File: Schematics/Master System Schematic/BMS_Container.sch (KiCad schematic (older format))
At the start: 8 parts, among them K1 Cooling Pump Shutoff Relay, K53 BMS_PWR_Relay, K54 Cooling Pump Relay, K55 BMS_Fan_Relay, U6 OrionBMS2

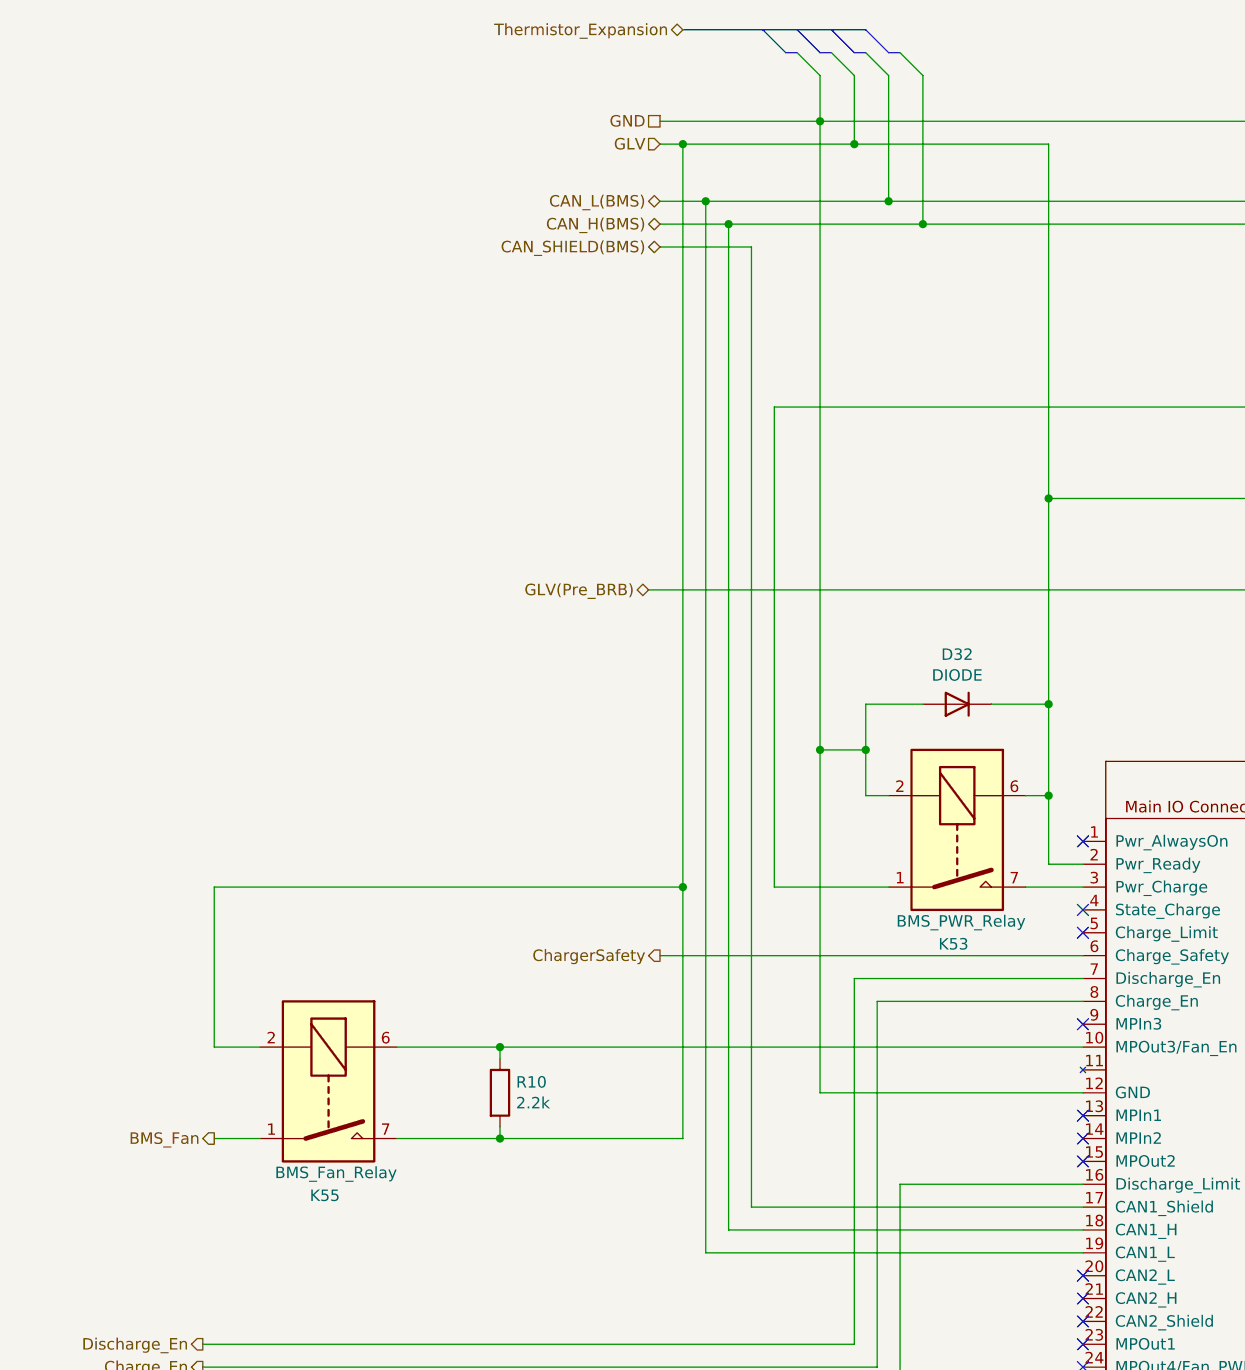
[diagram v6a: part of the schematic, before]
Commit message: Removed BMS fan
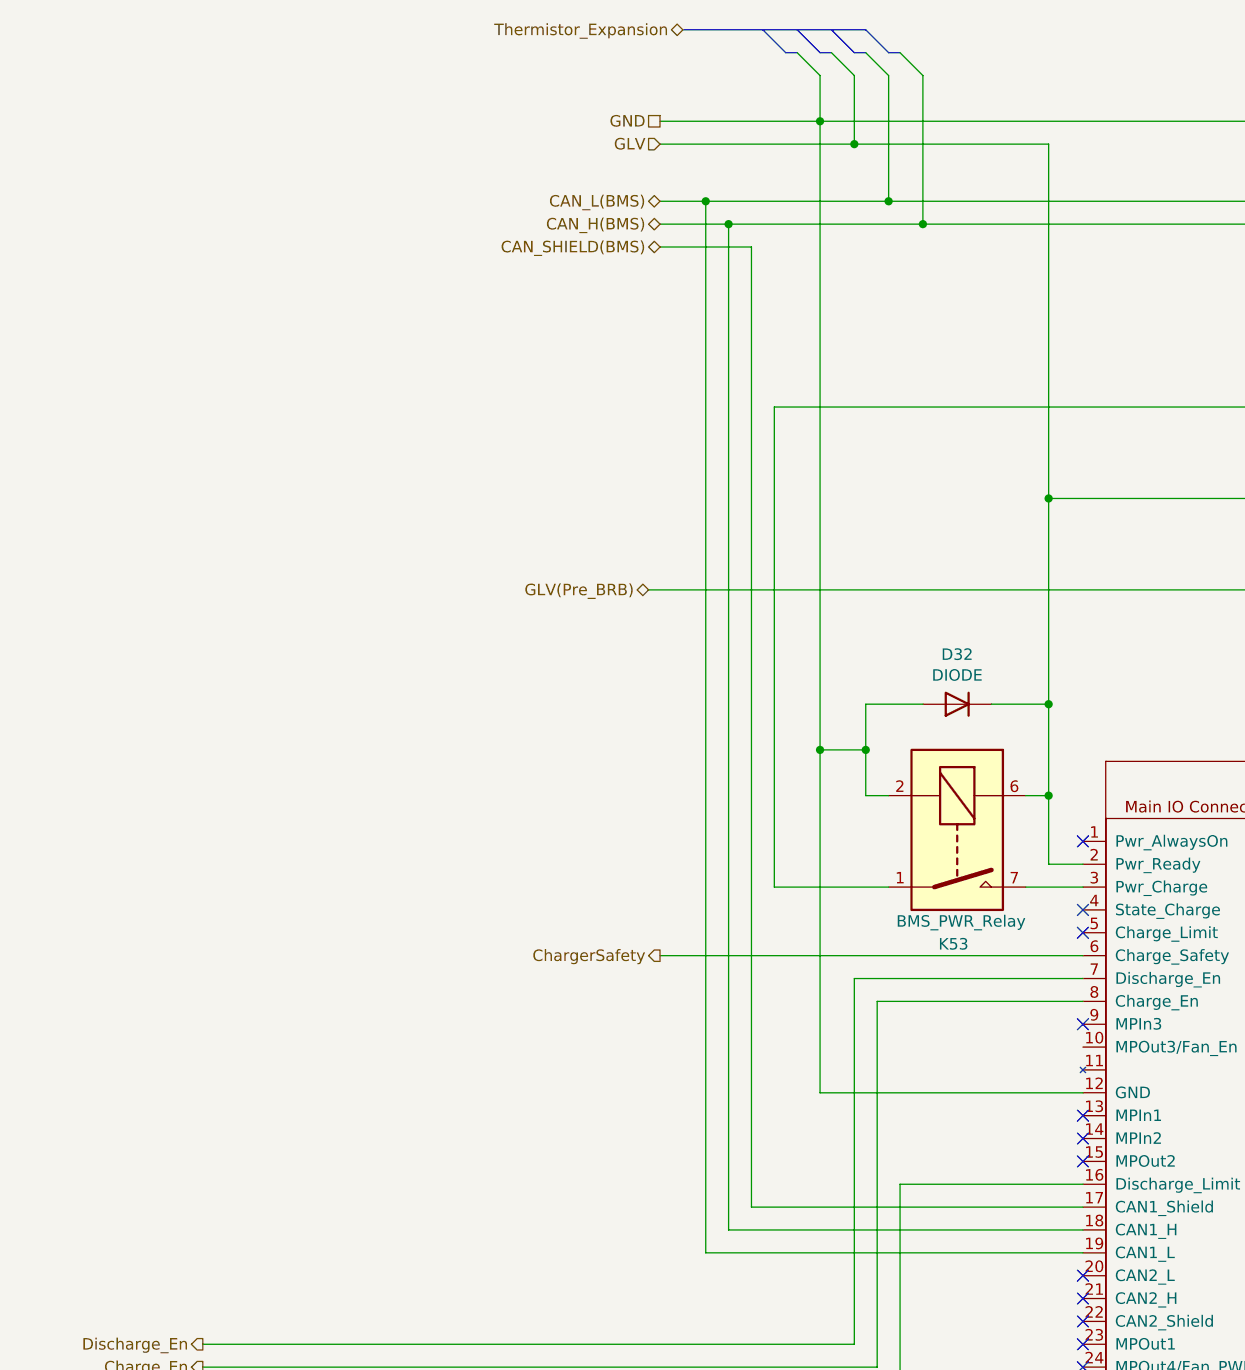
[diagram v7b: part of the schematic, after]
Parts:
- removed K55: BMS_Fan_Relay, Relay_THT:Relay_StandexMeder_DIP_LowProfile, symbol Relay:DIPxx-1Axx-11x
- removed R10: 2.2k, symbol Device:R
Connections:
- net at U6.3 (RM2+): now also K53.7, K53.8
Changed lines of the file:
@@
 	5550 1550 5550 4300
 Connection ~ 5550 1550
-Wire Wire Line
-	4850 1650 4950 1650
 Connection ~ 6550 4100
 Wire Wire Line
@@
 Wire Wire Line
 	8000 1650 8000 2800
-Wire Wire Line
-	6700 5600 4150 5600
-Text HLabel 2900 6000 0    50   Output ~ 0
-BMS_Fan
-Wire Wire Line
-	3100 6000 2900 6000
-Wire Wire Line
-	3700 6000 4150 6000
-Wire Wire Line
-	4950 6000 4950 4900
-Connection ~ 4950 1650
-$Comp
-L Device:R R10
-U 1 1 64558B5B
-P 4150 5800
-F 0 "R10" H 4220 5846 50  0000 L CNN
-F 1 "2.2k" H 4220 5755 50  0000 L CNN
-F 2 "" V 4080 5800 50  0001 C CNN
-F 3 "~" H 4150 5800 50  0001 C CNN
-	1    4150 5800
-	1    0    0    -1
-$EndComp
-Wire Wire Line
-	4150 5650 4150 5600
-Connection ~ 4150 5600
-Wire Wire Line
-	4150 5600 3700 5600
-Wire Wire Line
-	4150 5950 4150 6000
-Connection ~ 4150 6000
-Wire Wire Line
-	4150 6000 4950 6000
-Wire Wire Line
-	3100 5600 2900 5600
-Wire Wire Line
-	2900 5600 2900 4900
-Wire Wire Line
-	2900 4900 4950 4900
-Connection ~ 4950 4900
-Wire Wire Line
-	4950 4900 4950 1650
-$Comp
-L Relay:DIPxx-1Axx-11x K55
-U 1 1 5FB9D72C
-P 3400 5800
-F 0 "K55" V 3850 5850 50  0000 R CNN
-F 1 "BMS_Fan_Relay" V 3750 6100 50  0000 R CNN
-F 2 "Relay_THT:Relay_StandexMeder_DIP_LowProfile" H 3750 5750 50  0001 L CNN
-F 3 "https://standexelectronics.com/wp-content/uploads/datasheet_reed_relay_DIP.pdf" H 3400 5800 50  0001 C CNN
-	1    3400 5800
-	0    1    1    0
-$EndComp
 Wire Wire Line
 	8350 3200 6550 3200
@@
 Wire Wire Line
 	8000 1650 14100 1650
-Wire Wire Line
-	4950 1650 5700 1650
 Wire Wire Line
 	5150 2000 6000 2000
@@
 Wire Wire Line
 	5900 7100 2850 7100
+Text HLabel 2850 6900 0    50   Output ~ 0
+Discharge_En
+Text HLabel 2850 7000 0    50   Output ~ 0
+Charge_En
+Text HLabel 2850 7100 0    50   Output ~ 0
+Discharge_Limit
 Wire Bus Line
 	8850 8500 8850 8800
@@
 Wire Bus Line
 	4950 1150 5750 1150
-Text HLabel 2850 6900 0    50   Output ~ 0
-Discharge_En
-Text HLabel 2850 7000 0    50   Output ~ 0
-Charge_En
-Text HLabel 2850 7100 0    50   Output ~ 0
-Discharge_Limit
+Wire Wire Line
+	4850 1650 5700 1650
 $EndSCHEMATC

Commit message: starting BMS redraw
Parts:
- removed D31: DIODE, symbol Simulation_SPICE:DIODE
- added D?: DIODE, symbol Simulation_SPICE:DIODE
- added K? (x2): Charging Isolation Relay, Relay_THT:Relay_StandexMeder_DIP_LowProfile, symbol Relay:DIPxx-1Axx-11x
- added K?: BMS_PWR_Relay, Relay_THT:Relay_StandexMeder_DIP_LowProfile, symbol Relay:DIPxx-1Axx-11x
- added K?: Cooling Pump Relay, Relay_THT:Relay_StandexMeder_DIP_LowProfile, symbol Relay:DIPxx-1Axx-11x
- added K?: Cooling Pump Shutoff Relay, Relay_THT:Relay_SPST_StandexMeder_MS_Form1AB, symbol Relay:MSxx-1Bxx-75
- added U?: OrionBMS2, symbol NER:OrionBMS2
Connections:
- wire segments 88 -> 188
- no-connect marks 22 -> 44
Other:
- moved on the sheet: D32, K1, K53, K54, U6
